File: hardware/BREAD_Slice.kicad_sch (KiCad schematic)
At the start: 15 parts, among them J1 Conn_01x10_Female, J2 I2C_01x04

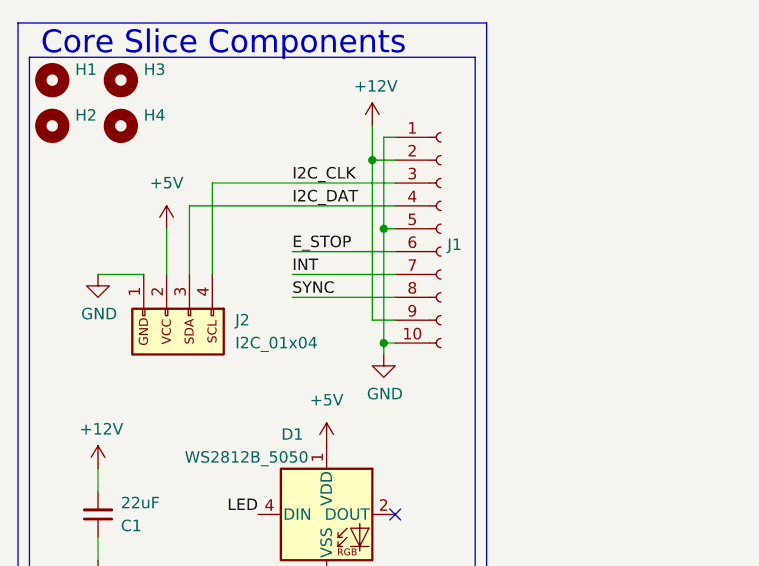
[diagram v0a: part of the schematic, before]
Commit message: fixed 5-12V converter reinitializing placement when pcb is updated
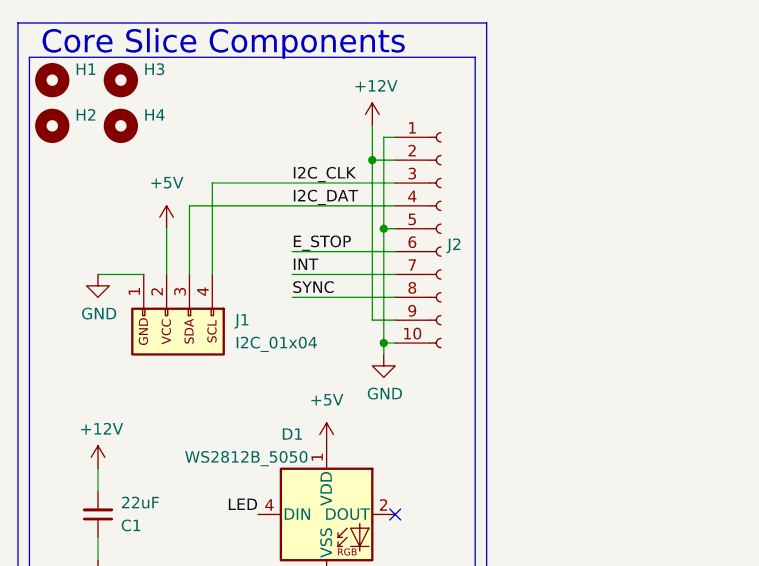
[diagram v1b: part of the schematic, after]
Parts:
- HS1: footprint SparkFun-Fuse:Thermal Pad -> KML-Custom:Thermal Pad
- renumbered J2 to J1, J1 to J2
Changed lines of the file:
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@@
 		(on_board yes)
 		(dnp no)
-		(property "Reference" "J1"
+		(property "Reference" "J2"
 			(at 61.6712 38.608 0)
 			(effects
@@
 			(project "BREAD_Slice"
 				(path "/66043bca-a260-4915-9fce-8a51d324c687"
-					(reference "J1")
+					(reference "J2")
 					(unit 1)
 				)
@@
 			)
 		)
-		(property "Footprint" "SparkFun-Fuse:Thermal Pad"
+		(property "Footprint" "KML-Custom:Thermal Pad"
 			(at 45.72 112.0648 0)
 			(effects
@@
 		(dnp no)
 		(fields_autoplaced yes)
-		(property "Reference" "J2"
+		(property "Reference" "J1"
 			(at 38.1 46.99 90)
 			(effects
@@
 			(project "BREAD_Slice"
 				(path "/66043bca-a260-4915-9fce-8a51d324c687"
-					(reference "J2")
-					(unit 1)
-				)
+					(reference "J1")
+					(unit 1)
+				)
